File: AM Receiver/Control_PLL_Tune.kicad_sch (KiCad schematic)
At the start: 22 parts, among them IC101 SA612AD, IC102 74HC74D, IC104 74HCT4046AD, P102 50k 10% Trimmer

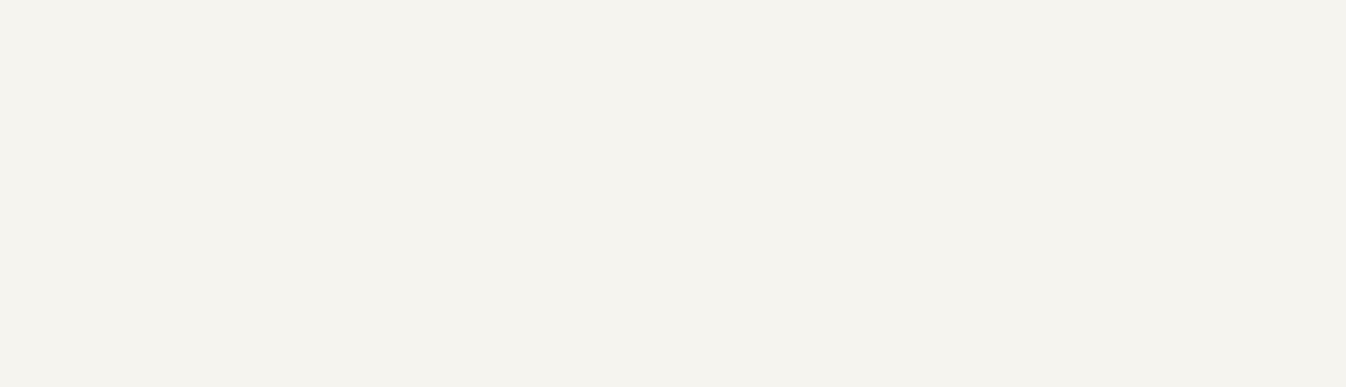
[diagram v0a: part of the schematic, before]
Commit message: Filled out information in User.Drawings on PCB
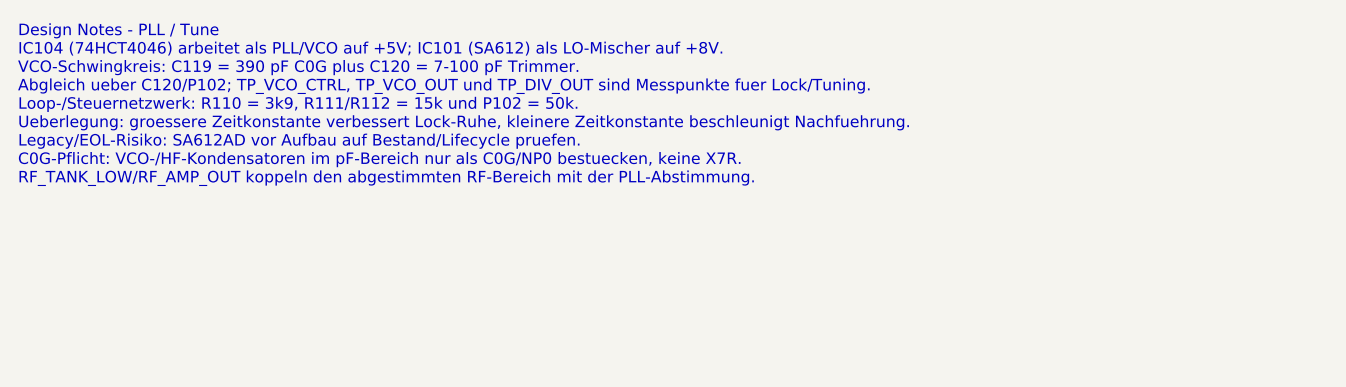
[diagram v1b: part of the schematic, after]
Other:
- note added: "Design Notes - PLL / Tune IC104 (74HCT4046) arbeitet als PLL/VCO auf +5V; IC101 (SA612) als LO-Mischer auf +8V. VCO-Schwingkreis: C119 = 390 pF C0G plus C120 = 7-100 pF Trimmer. Abgleich ueber C120/P102; TP_VCO_CTRL, TP_VCO_OUT und TP_DIV_OUT sind Messpunkte fuer Lock/Tuning. Loop-/Steuernetzwerk: R110 = 3k9, R111/R112 = 15k und P102 = 50k. Ueberlegung: groessere Zeitkonstante verbessert Lock-Ruh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"
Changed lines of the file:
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@@
 		(comment 3 "T. Brown")
+	)
+	(text "Design Notes - PLL / Tune\nIC104 (74HCT4046) arbeitet als PLL/VCO auf +5V; IC101 (SA612) als LO-Mischer auf +8V.\nVCO-Schwingkreis: C119 = 390 pF C0G plus C120 = 7-100 pF Trimmer.\nAbgleich ueber C120/P102; TP_VCO_CTRL, TP_VCO_OUT und TP_DIV_OUT sind Messpunkte fuer Lock/Tuning.\nLoop-/Steuernetzwerk: R110 = 3k9, R111/R112 = 15k und P102 = 50k.\nUeberlegung: groessere Zeitkonstante verbessert Lock-Ruhe, kleinere Zeitkonstante beschleunigt Nachfuehrung.\nLegacy/EOL-Risiko: SA612AD vor Aufbau auf Bestand/Lifecycle pruefen.\nC0G-Pflicht: VCO-/HF-Kondensatoren im pF-Bereich nur als C0G/NP0 bestuecken, keine X7R.\nRF_TANK_LOW/RF_AMP_OUT koppeln den abgestimmten RF-Bereich mit der PLL-Abstimmung."
+		(exclude_from_sim no)
+		(at 35.56 34.29 0)
+		(effects
+			(font
+				(size 1.27 1.27)
+			)
+			(justify left)
+		)
 	)
 	(junction

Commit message: Updated User.drawing information and Design Review
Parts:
- IC101: ProcurementNote (none) -> Legacy/EOL risk for SA612AD/01,118; verify stock/lifecycle 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
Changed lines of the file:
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@@
+			)
+		)
+		(property "ProcurementNote" "Legacy/EOL risk for SA612AD/01,118; verify stock/lifecycle and approved substitute before build."
+			(at 80.01 100.33 0)
+			(hide yes)
+			(show_name no)
+			(do_not_autoplace no)
+			(effects
+				(font
+					(size 1.27 1.27)
+				)
 			)
 		)

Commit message: Updated Design notes in schematic
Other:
- note added: "Design Notes - PLL / Tune IC104 (74HCT4046) arbeitet als PLL/VCO auf +5V; IC101 (SA612) als LO-Mischer auf +8V. VCO-Schwingkreis: C119 = 390 pF C0G plus C120 = 7-100 pF Trimmer. Abgleich über C120/P102; TP_VCO_CTRL, TP_VCO_OUT und TP_DIV_OUT sind Messpunkte für Lock/Tuning. Loop-/Steuernetzwerk: R110 = 3k9, R111/R112 = 15k und P102 = 50k. Überlegung: groeßere Zeitkonstante verbessert Lock-Ruhe, k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"
- note removed: "Design Notes - PLL / Tune IC104 (74HCT4046) arbeitet als PLL/VCO auf +5V; IC101 (SA612) als LO-Mischer auf +8V. VCO-Schwingkreis: C119 = 390 pF C0G plus C120 = 7-100 pF Trimmer. Abgleich ueber C120/P102; TP_VCO_CTRL, TP_VCO_OUT und TP_DIV_OUT sind Messpunkte fuer Lock/Tuning. Loop-/Steuernetzwerk: R110 = 3k9, R111/R112 = 15k und P102 = 50k. Ueberlegung: groessere Zeitkonstante verbessert Lock-Ruh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"
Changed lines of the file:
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@@
 		(comment 3 "T. Brown")
 	)
-	(text "Design Notes - PLL / Tune\nIC104 (74HCT4046) arbeitet als PLL/VCO auf +5V; IC101 (SA612) als LO-Mischer auf +8V.\nVCO-Schwingkreis: C119 = 390 pF C0G plus C120 = 7-100 pF Trimmer.\nAbgleich ueber C120/P102; TP_VCO_CTRL, TP_VCO_OUT und TP_DIV_OUT sind Messpunkte fuer Lock/Tuning.\nLoop-/Steuernetzwerk: R110 = 3k9, R111/R112 = 15k und P102 = 50k.\nUeberlegung: groessere Zeitkonstante verbessert Lock-Ruhe, kleinere Zeitkonstante beschleunigt Nachfuehrung.\nLegacy/EOL-Risiko: SA612AD vor Aufbau auf Bestand/Lifecycle pruefen.\nC0G-Pflicht: VCO-/HF-Kondensatoren im pF-Bereich nur als C0G/NP0 bestuecken, keine X7R.\nRF_TANK_LOW/RF_AMP_OUT koppeln den abgestimmten RF-Bereich mit der PLL-Abstimmung."
+	(text "Design Notes - PLL / Tune\nIC104 (74HCT4046) arbeitet als PLL/VCO auf +5V; IC101 (SA612) als LO-Mischer auf +8V.\nVCO-Schwingkreis: C119 = 390 pF C0G plus C120 = 7-100 pF Trimmer.\nAbgleich über C120/P102; TP_VCO_CTRL, TP_VCO_OUT und TP_DIV_OUT sind Messpunkte für Lock/Tuning.\nLoop-/Steuernetzwerk: R110 = 3k9, R111/R112 = 15k und P102 = 50k.\nÜberlegung: groeßere Zeitkonstante verbessert Lock-Ruhe, kleinere Zeitkonstante beschleunigt Nachführung.\nLegacy/EOL-Risiko: SA612AD vor Aufbau auf Bestand/Lifecycle prüfen.\nC0G-Pflicht: VCO-/HF-Kondensatoren im pF-Bereich nur als C0G/NP0 bestücken, keine X7R.\nRF_TANK_LOW/RF_AMP_OUT koppeln den abgestimmten RF-Bereich mit der PLL-Abstimmung."
 		(exclude_from_sim no)
 		(at 35.56 34.29 0)
